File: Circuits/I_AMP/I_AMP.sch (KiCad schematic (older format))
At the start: 44 parts, among them P1 INPUT, P2 +8, P3 -8, P4 GND, P5 GAIN_ADJ., P6 OUTPUT (0-5V), U1 TL062, U2 LM393, U3 OPA277

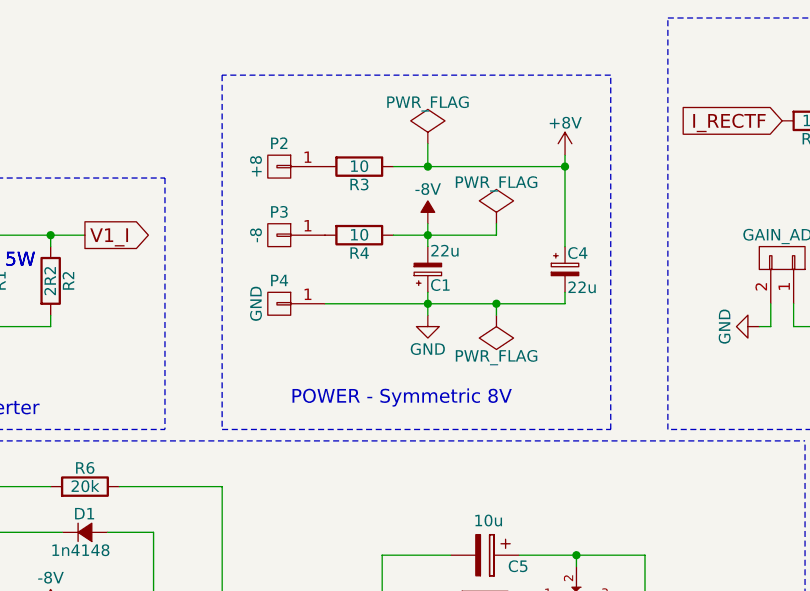
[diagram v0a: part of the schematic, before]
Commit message: ADD: Current Amplifier Complete PCB Design
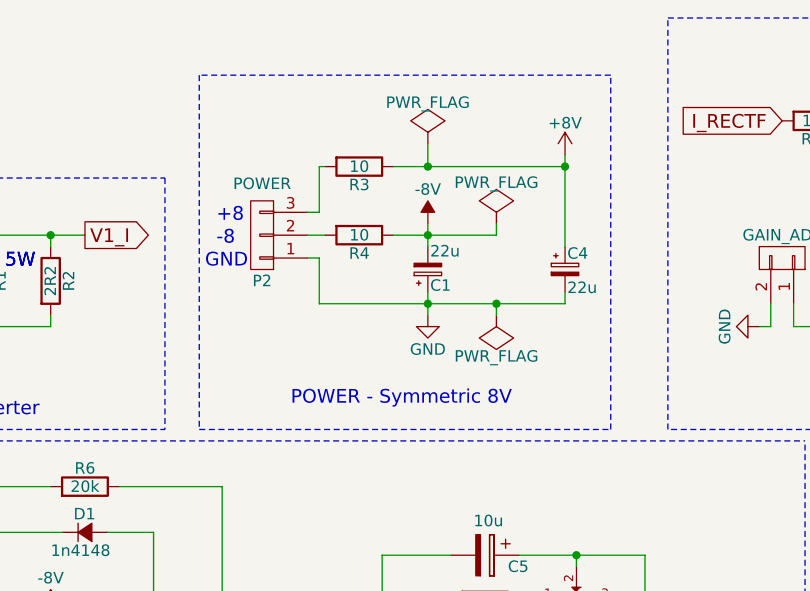
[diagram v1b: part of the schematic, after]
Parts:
- removed P2: +8, symbol CONN_01X01
- removed P3: -8, symbol CONN_01X01
- removed P4: GND, symbol CONN_01X01
- added P2: POWER, Connectors:bornier3, symbol CONN_01X03
- C1, C4, C5: footprint (none) -> Capacitors_THT:CP_Radial_D5.0mm_P2.50mm
- C2, C3, C6, C7, C8, C9: footprint (none) -> Capacitors_THT:C_Rect_L7.0mm_W2.5mm_P5.00mm
- D1, D2, D3: footprint (none) -> Diodes_THT:D_DO-35_SOD27_P7.62mm_Horizontal
- D4: footprint (none) -> LEDs:LED_D5.0mm
- D5: footprint (none) -> Diodes_THT:D_DO-41_SOD81_P7.62mm_Horizontal
- P1, P6: footprint (none) -> Connectors:bnc-ci
- P5: footprint (none) -> w_pin_strip:pin_strip_2mm_2
- R1, R2: footprint (none) -> Resistors_THT:R_Axial_DIN0617_L17.0mm_D6.0mm_P20.32mm_Horizontal
- R10, R11, R12, R13, R14, R15, R16, R17, R18, R19, R5, R6, R7, R8, R9: footprint (none) -> w_pth_resistors:RC03
- R3, R4: footprint (none) -> Resistors_THT:R_Axial_DIN0309_L9.0mm_D3.2mm_P12.70mm_Horizontal
- RV1, RV2: footprint (none) -> Potentiometers:Potentiometer_Alps_RK163_Single_Vertical
- U1, U2, U3: footprint (none) -> Housings_DIP:DIP-8_W7.62mm_Socket_LongPads
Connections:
- net GND: now also P2.1 (P1)
- net at R3.2: now also P2.3 (P3)
- net at R4.2: now also P2.2 (P2)
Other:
- note added: "+8"
- note added: "-8"
- note added: "GND"

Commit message: EDIT: REORGANIZING FILES
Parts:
- C1, C4: symbol CP_Small -> I_AMP-rescue:CP_Small
- C2, C3, C6, C7: symbol C_Small -> I_AMP-rescue:C_Small
- C5: symbol CP -> I_AMP-rescue:CP
- C8, C9: symbol C -> I_AMP-rescue:C
- D1, D2, D3: symbol D_Small -> I_AMP-rescue:D_Small
- D4: symbol LED -> I_AMP-rescue:LED
- D5: symbol ZENERsmall -> I_AMP-rescue:ZENERsmall
- P1, P6: symbol BNC -> I_AMP-rescue:BNC
- P2: symbol CONN_01X03 -> I_AMP-rescue:CONN_01X03
- P5: symbol CONN_01X02 -> I_AMP-rescue:CONN_01X02
- R1, R10, R11, R12, R13, R14, R15, R16, R17, R18, R19, R2, R3, R4, R5, R6, R7, R8, R9: symbol R -> I_AMP-rescue:R
- RV1, RV2: symbol POT -> I_AMP-rescue:POT
- U1: symbol TL062 -> I_AMP-rescue:TL062
- U2: symbol LM393 -> I_AMP-rescue:LM393
- U3: symbol OPA177 -> I_AMP-rescue:OPA177
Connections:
- no-connect marks 10 -> 8
